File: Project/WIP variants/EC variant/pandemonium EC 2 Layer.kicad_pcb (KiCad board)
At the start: 2 copper layers, 190.5 x 81.6 mm, 106 parts, among them J1 USB_C_Receptacle_USB2.0, SW1 DFU, U11 PRTR5V0U2X, U5 OPA354, U6 74HC4051, U7 74HC4051, U8 STM32F072CBT6, U9 XC6206PxxxMR-Regulator_Linear

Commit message: production files EC
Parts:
- H1, H10, H11, H12, H13, H14, H16, H18, H19, H2, H20, H23, H24, H25, H3, H4, H5, H6, H7, H8, H9: footprint cipulot_parts:HOLE_M2 -> cipulot_parts:HOLE_M2 (no arrow)
- moved G*** 93.8 mm to (127.0, 71.4)
- moved G*** 0.30 mm to (206.7, 102.4)
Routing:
- net GND: track 74.4 -> 77.3 mm, vias 192 -> 194
- net COL4: track 101.8 -> 98.9 mm, vias 4 -> 0
- net COL0: track 92.6 -> 92.4 mm, vias 4 -> 0
- net COL9: track 112.3 -> 112.2 mm, vias 5 -> 0
- net ROW3: vias 10 -> 1
- net ROW2: vias 14 -> 4
- net ROW1: vias 15 -> 5
- net ROW0: vias 13 -> 3
- net COL8: vias 4 -> 2
- net COL7: vias 6 -> 2
- net COL6: vias 3 -> 0
- net COL5: vias 5 -> 0
- net COL3: vias 5 -> 0
- net COL2: vias 3 -> 0
- net COL1: vias 4 -> 0
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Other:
- board text added: "125"
- board text added: "150"
- board text added: "175"
- board text added: "225"
- board text removed: "1.25"
- board text removed: "1.75"
- board text removed: "2.25"

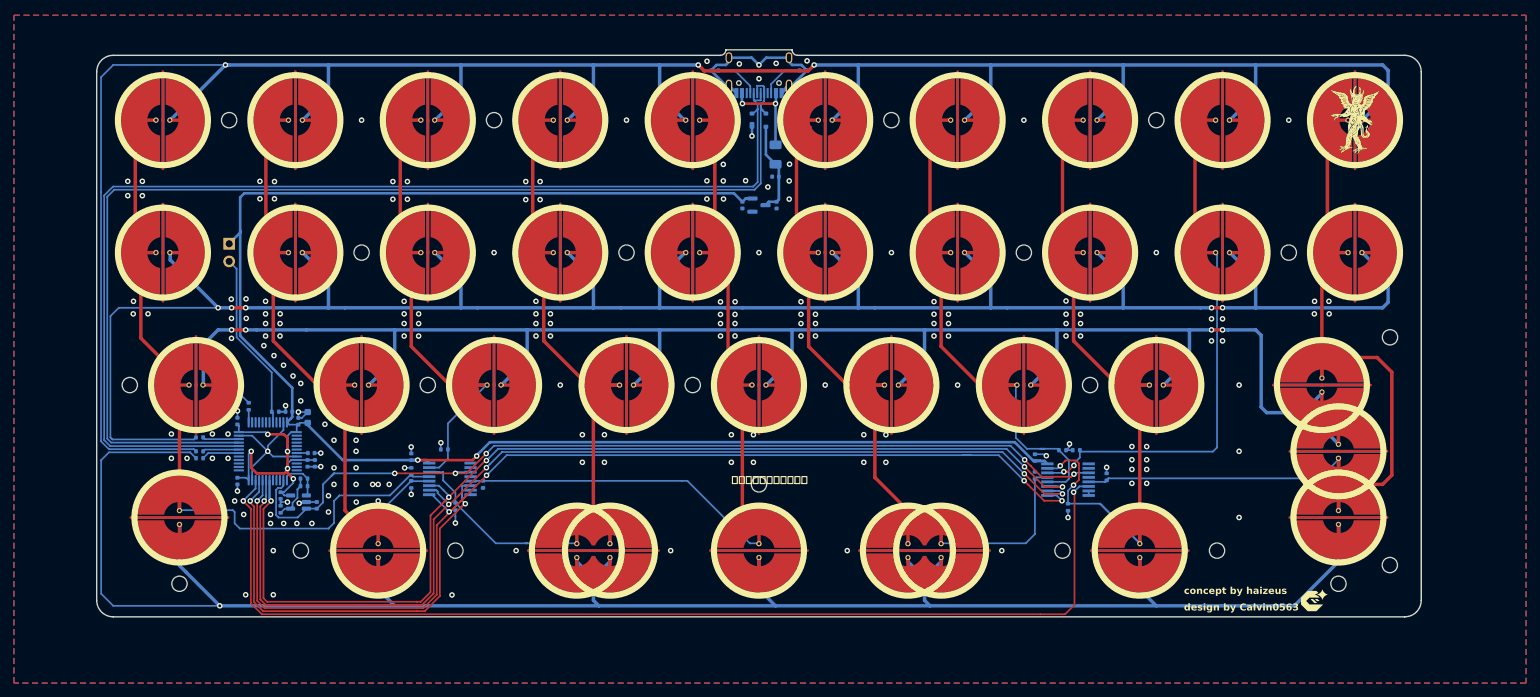
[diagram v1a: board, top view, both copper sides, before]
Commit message: EC 2 layer production files
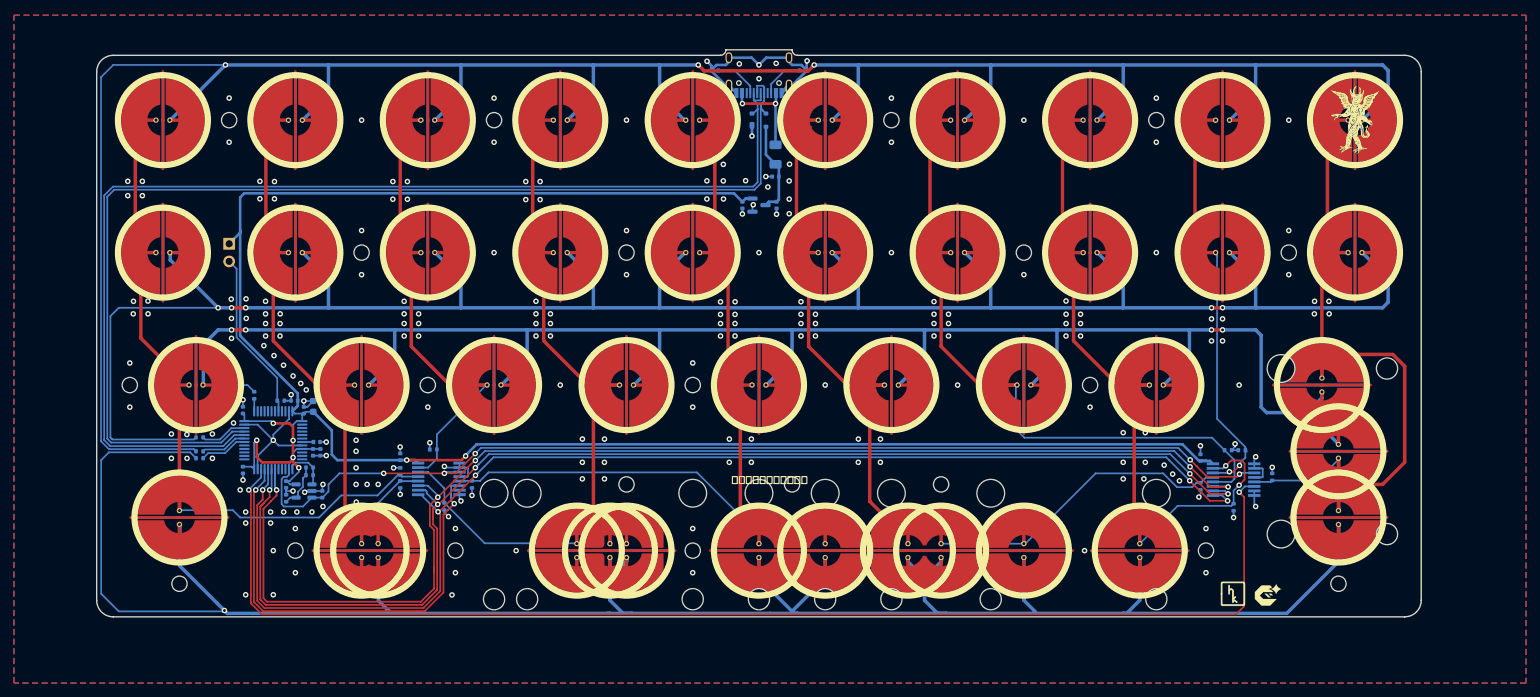
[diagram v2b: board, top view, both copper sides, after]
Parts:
- removed the G*** at (206.7, 102.4)
- removed H13, H25: MountingHole, cipulot_parts:HOLE_M2 (no arrow)
- added G***: LOGO, LOGO, F.Cu at (200.0, 101.6)
- added G***: LOGO, LOGO, F.Cu at (195.3, 101.6)
- added G***: LOGO, LOGO, B.Cu at (184.2, 49.2)
- added G***: LOGO, LOGO, B.Cu at (165.1, 49.2)
- added H15: MountingHole, cipulot_parts:HOLE_M2 (no arrow), F.Cu at (108.0, 85.7)
- added H17: MountingHole, cipulot_parts:HOLE_M2 (no arrow), F.Cu at (117.5, 95.2)
- added S1: 225, PCM_marbastlib-mx:STAB_MX_2.25u, F.Cu at (105.6, 95.2)
- added S2: 225, PCM_marbastlib-mx:STAB_MX_2.25u, F.Cu at (148.4, 95.2)
- added S3: 225, PCM_marbastlib-mx:STAB_MX_ISO-ROT, F.Cu at (210.3, 81.0)
- added S4: 3, PCM_marbastlib-mx:STAB_MX_3u, F.Cu at (108.0, 95.2)
- added S5: 3, PCM_marbastlib-mx:STAB_MX_3u, F.Cu at (165.1, 95.2)
- added SW_EC34: Topre, cipulot_parts:ecs_pad_1U_no_ring_1u_edge_cut_horizontal, F.Cu at (136.5, 95.2)
- added SW_EC40: Topre, cipulot_parts:ecs_pad_1U_no_ring, F.Cu at (165.1, 95.2)
- SW_EC32: footprint cipulot_parts:ecs_pad_1U_no_ring -> cipulot_parts:ecs_pad_no_ring_1u&1.25u&1.5u
- SW_EC33: footprint cipulot_parts:ecs_pad_no_ring_stepped&normal -> cipulot_parts:ecs_pad_0.25U_0.125U_spaced_no_ring_cut_right
- SW_EC36: footprint cipulot_parts:ecs_pad_no_ring_stepped&normal -> cipulot_parts:ecs_pad_no_ring_stepped&normal_cut
- moved H24 40.0 mm to (131.8, 85.7)
- moved H16 26.2 mm to (153.2, 85.7)
- moved R24 23.9 mm to (190.5, 86.0), turned to -90 degrees
- moved C32 23.8 mm to (190.5, 81.9)
- moved G*** 23.8 mm to (127.0, 95.2)
- moved R25 23.8 mm to (196.4, 80.8)
- moved R26 23.8 mm to (195.3, 89.0)
- moved R27 23.8 mm to (194.5, 80.8)
- moved R28 23.8 mm to (200.8, 84.6)
- moved U7 23.8 mm to (195.3, 85.0)
- moved SW_EC32 2.38 mm to (69.8, 95.2), turned to 0 degrees
- moved C33 1.77 mm to (61.5, 75.1)
- moved C38 1.77 mm to (52.8, 83.7)
- moved U5 1.77 mm to (61.6, 86.7)
- moved C30 1.77 mm to (64.2, 87.1)
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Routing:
- net ROW3: track 280.7 -> 321.3 mm
- net AMUX_SEL_1: track 159.2 -> 186.4 mm
- net APLEX_EN_PIN_1: track 157.3 -> 183.3 mm
- net AMUX_SEL_0: track 162.4 -> 187.0 mm
- net +3V3: track 275.4 -> 298.7 mm
- net AMUX_SEL_2: track 162.1 -> 185.2 mm
- net GND: track 77.3 -> 100.5 mm, vias 194 -> 229
- net COL5: track 91.8 -> 114.5 mm
- net COL6: track 63.9 -> 86.4 mm
- net COL9: track 112.2 -> 91.1 mm
- net APLEX_OUT: track 133.4 -> 154.1 mm
- net COL8: track 71.8 -> 54.6 mm
- net COL7: track 96.2 -> 87.8 mm
- net COL0: track 92.4 -> 86.7 mm
- net COL4: track 98.9 -> 102.3 mm
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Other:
- board text added: "&calvin0563"
- board text added: "*requires plate stabs"
- board text added: "3"
- board text added: "6"
- board text added: "7*"
- board text removed: "&Calvin0563"
- board text removed: "7"
- board text removed: "concept by haizeus"
- board text removed: "design by Calvin0563"

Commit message: BLE & EC edited
requires production files!!
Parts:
- removed C44: 100nF, Capacitor_SMD:C_0402_1005Metric
- removed F3: ASMD1206-150, Fuse:Fuse_1206_3216Metric
- removed J1: USB_C_Receptacle_USB2.0, Connector_USB:USB_C_Receptacle_HRO_TYPE-C-31-M-12
- removed R29, R30: 5.1k, Resistor_SMD:R_0402_1005Metric
- removed U11: PRTR5V0U2X, Package_TO_SOT_SMD:SOT-143
- added J2: SM04B, Connector_JST:JST_SH_SM04B-SRSS-TB_1x04-1MP_P1.00mm_Horizontal, B.Cu at (88.1, 42.9)
- moved C41 57.2 mm to (72.4, 45.2)
- moved C42 57.2 mm to (67.5, 45.2)
- moved U9 57.2 mm to (69.8, 45.2)
- moved C29 0.20 mm to (59.0, 85.5)
- moved C32 0.20 mm to (190.5, 81.7)
- moved C33 0.20 mm to (61.5, 74.9)
- moved C35 0.20 mm to (52.8, 74.8)
- moved C36 0.20 mm to (60.2, 73.5)
- moved C37 0.20 mm to (62.9, 74.3)
- moved C38 0.20 mm to (52.8, 83.5)
- moved H10 0.20 mm to (79.4, 71.2)
- moved H11 0.20 mm to (117.5, 71.2)
- moved H12 0.20 mm to (174.6, 71.2)
- moved H14 0.20 mm to (60.3, 95.0)
- moved H17 0.20 mm to (117.5, 95.0)
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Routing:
- net D_P: track 168.4 -> 108.7 mm
- net +3V3: track 298.7 -> 241.5 mm
- net D_N: track 167.3 -> 110.3 mm
- net GND: track 100.5 -> 67.9 mm, vias 229 -> 222
- net VBUS: track 13.8 -> 0.00 mm, vias 2 -> 0
- net +5V: track 13.5 -> 23.7 mm
- net Net-(J1-CC1): track 6.54 -> 0.00 mm
- net Net-(J1-CC2): track 6.20 -> 0.00 mm
- net ROW0: track 349.2 -> 348.5 mm, vias 3 -> 1
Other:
- board size 190.5 x 81.6 mm -> 190.5 x 80.8 mm
